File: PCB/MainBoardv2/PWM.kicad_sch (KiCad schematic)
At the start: 14 parts, among them J11 Conn_01x03_Socket, J12 Conn_01x03_Socket, J13 Conn_01x04_Socket, J14 Conn_01x03_Socket, J15 Conn_01x03_Socket, J16 Conn_01x04_Socket, J17 Conn_01x03_Socket, J18 Conn_01x03_Socket, J19 Conn_01x04_Socket, J20 Conn_01x03_Socket, SW3 Slide

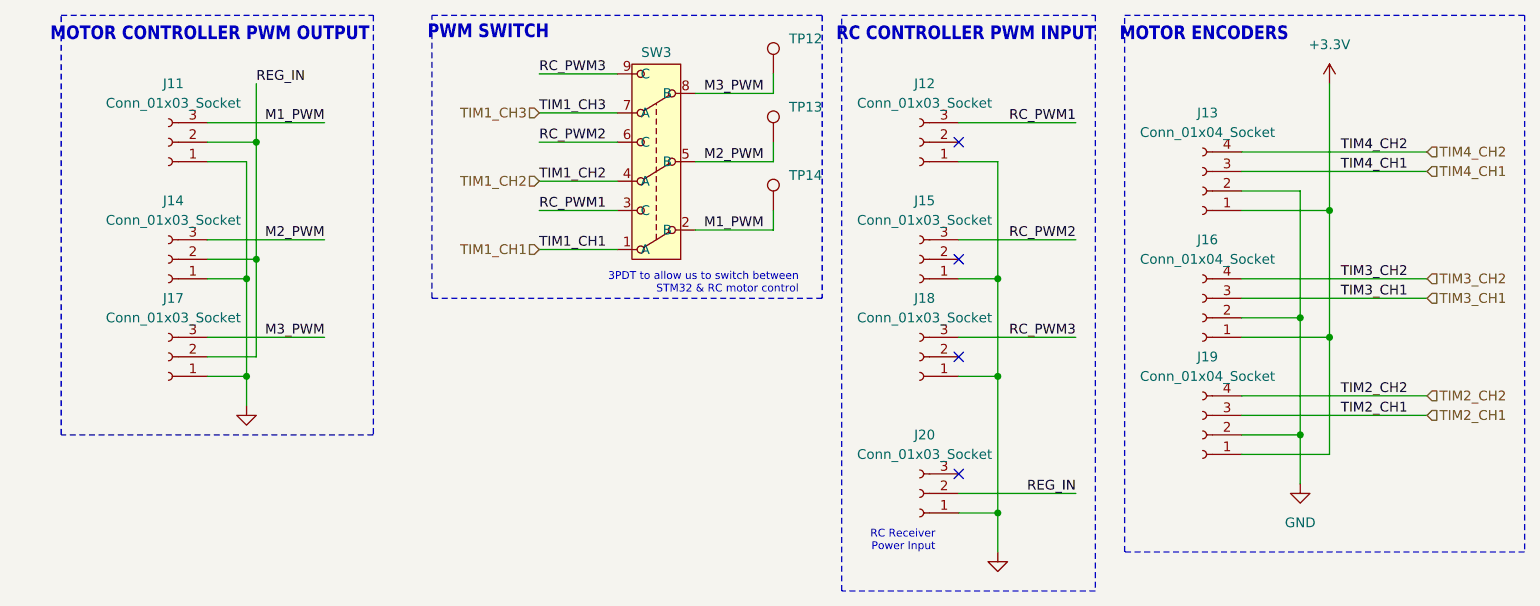
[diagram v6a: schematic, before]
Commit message: Main Board v2 Rough component layout complete
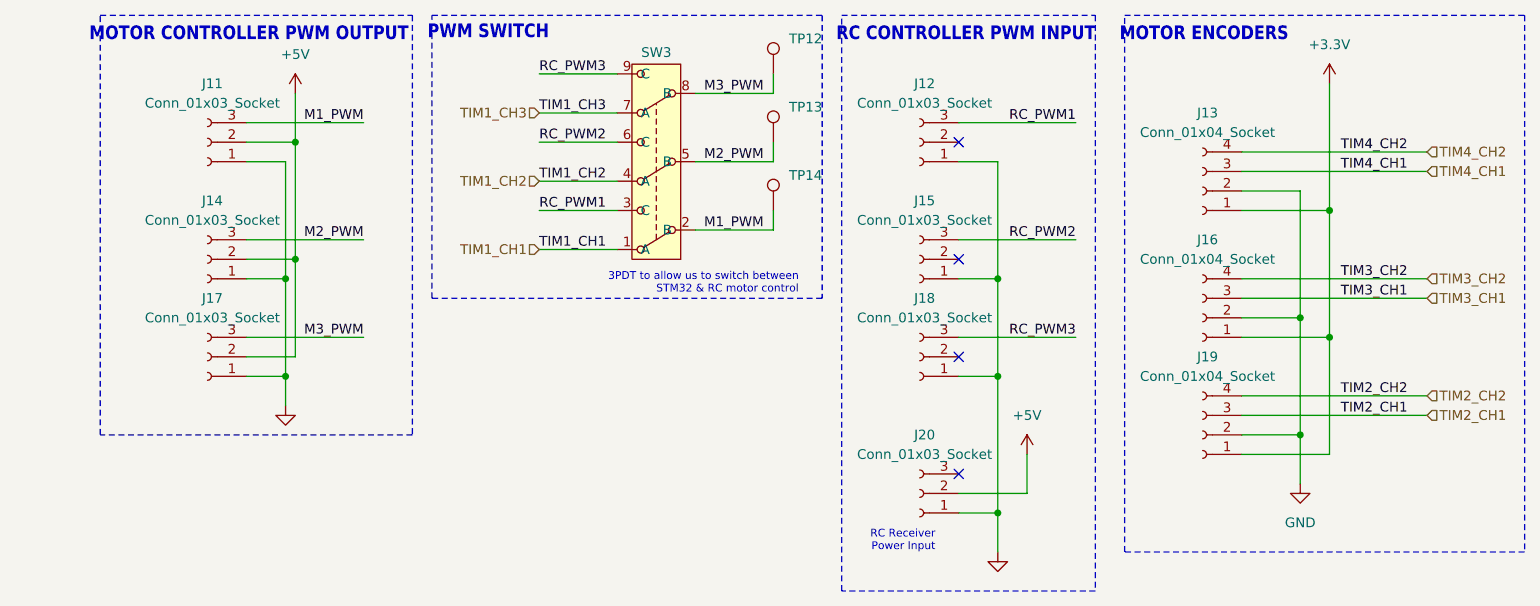
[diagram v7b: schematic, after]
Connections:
- net REG_IN renamed +5V
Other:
- moved on the sheet: J11, J14, J17

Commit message: updating layout progress, adding limit switch extra circuitry
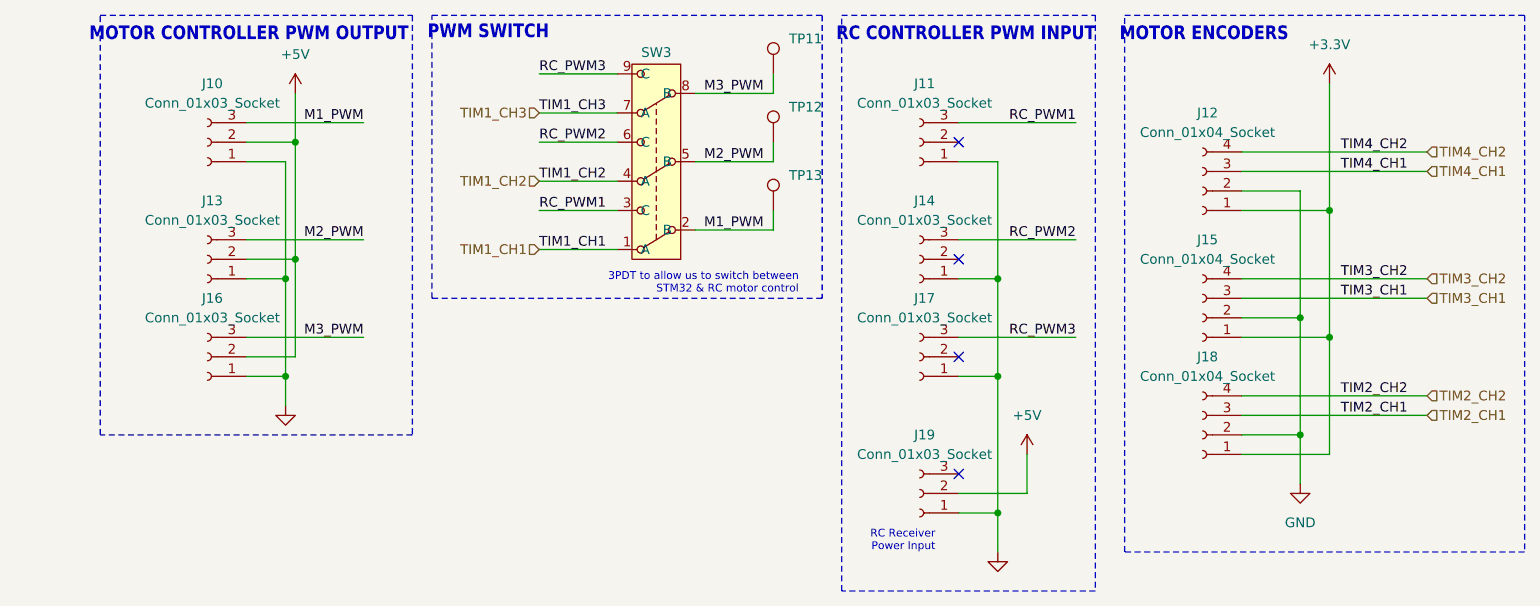
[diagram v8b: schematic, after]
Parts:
- J10: renamed from J11; footprint Connector_PinHeader_2.54mm:PinHeader_1x03_P2.54mm_Vertical -> Connector_PinHeader_2.54mm:PinHeader_1x03_P2.54mm_Horizontal
- J13: renamed from J14; footprint Connector_PinHeader_2.54mm:PinHeader_1x03_P2.54mm_Vertical -> Connector_PinHeader_2.54mm:PinHeader_1x03_P2.54mm_Horizontal
- J16: renamed from J17; footprint Connector_PinHeader_2.54mm:PinHeader_1x03_P2.54mm_Vertical -> Connector_PinHeader_2.54mm:PinHeader_1x03_P2.54mm_Horizontal
- renumbered J12 to J11, J13 to J12, J15 to J14, J16 to J15, J18 to J17, J19 to J18, J20 to J19, TP12 to TP11, TP13 to TP12, TP14 to TP13
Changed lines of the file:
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@@
 		(dnp no)
 		(fields_autoplaced yes)
-		(property "Reference" "J19"
+		(property "Reference" "J18"
 			(at 194.945 104.14 0)
 			(effects
@@
 			(project "MainBoardv2"
 				(path "/d9c43b87-8960-41bd-bfcc-9c305bab2f72/cc711eab-7295-453b-97e2-e692aa39ee0f"
-					(reference "J19")
+					(reference "J18")
 					(unit 1)
 				)
@@
 		(dnp no)
 		(fields_autoplaced yes)
-		(property "Reference" "#PWR040"
+		(property "Reference" "#PWR036"
 			(at 76.2 73.66 0)
 			(effects
@@
 			(project "MainBoardv2"
 				(path "/d9c43b87-8960-41bd-bfcc-9c305bab2f72/cc711eab-7295-453b-97e2-e692aa39ee0f"
-					(reference "#PWR040")
+					(reference "#PWR036")
 					(unit 1)
 				)
@@
 		(dnp no)
 		(fields_autoplaced yes)
-		(property "Reference" "#PWR044"
+		(property "Reference" "#PWR040"
 			(at 167.64 135.89 0)
 			(effects
@@
 			(project "MainBoardv2"
 				(path "/d9c43b87-8960-41bd-bfcc-9c305bab2f72/cc711eab-7295-453b-97e2-e692aa39ee0f"
-					(reference "#PWR044")
+					(reference "#PWR040")
 					(unit 1)
 				)
@@
 		(on_board yes)
 		(dnp no)
-		(property "Reference" "J18"
+		(property "Reference" "J17"
 			(at 158.115 96.52 0)
 			(effects
@@
 			(project "MainBoardv2"
 				(path "/d9c43b87-8960-41bd-bfcc-9c305bab2f72/cc711eab-7295-453b-97e2-e692aa39ee0f"
-					(reference "J18")
+					(reference "J17")
 					(unit 1)
 				)
@@
 		(on_board yes)
 		(dnp no)
-		(property "Reference" "J17"
+		(property "Reference" "J16"
 			(at 65.405 96.52 0)
 			(effects
@@
 			)
 		)
-		(property "Footprint" "Connector_PinHeader_2.54mm:PinHeader_1x03_P2.54mm_Vertical"
+		(property "Footprint" "Connector_PinHeader_2.54mm:PinHeader_1x03_P2.54mm_Horizontal"
 			(at 64.77 104.14 0)
 			(effects
@@
 			(project "MainBoardv2"
 				(path "/d9c43b87-8960-41bd-bfcc-9c305bab2f72/cc711eab-7295-453b-97e2-e692aa39ee0f"
-					(reference "J17")
+					(reference "J16")
 					(unit 1)
 				)
@@
 		(dnp no)
 		(fields_autoplaced yes)
-		(property "Reference" "#PWR042"
+		(property "Reference" "#PWR038"
 			(at 171.45 120.65 0)
 			(effects
@@
 			(project "MainBoardv2"
 				(path "/d9c43b87-8960-41bd-bfcc-9c305bab2f72/cc711eab-7295-453b-97e2-e692aa39ee0f"
-					(reference "#PWR042")
+					(reference "#PWR038")
 					(unit 1)
 				)
@@
 		(dnp no)
 		(fields_autoplaced yes)
-		(property "Reference" "#PWR043"
+		(property "Reference" "#PWR039"
 			(at 207.01 127 0)
 			(effects
@@
 			(project "MainBoardv2"
 				(path "/d9c43b87-8960-41bd-bfcc-9c305bab2f72/cc711eab-7295-453b-97e2-e692aa39ee0f"
-					(reference "#PWR043")
+					(reference "#PWR039")
 					(unit 1)
 				)
@@
 		(on_board yes)
 		(dnp no)
-		(property "Reference" "J12"
+		(property "Reference" "J11"
 			(at 158.115 68.58 0)
 			(effects
@@
 			(project "MainBoardv2"
 				(path "/d9c43b87-8960-41bd-bfcc-9c305bab2f72/cc711eab-7295-453b-97e2-e692aa39ee0f"
-					(reference "J12")
+					(reference "J11")
 					(unit 1)
 				)
@@
 		(dnp no)
 		(fields_autoplaced yes)
-		(property "Reference" "#PWR041"
+		(property "Reference" "#PWR037"
 			(at 74.93 116.84 0)
 			(effects
@@
 			(project "MainBoardv2"
 				(path "/d9c43b87-8960-41bd-bfcc-9c305bab2f72/cc711eab-7295-453b-97e2-e692aa39ee0f"
-					(reference "#PWR041")
+					(reference "#PWR037")
 					(unit 1)
 				)
@@
 		(on_board yes)
 		(dnp no)
-		(property "Reference" "TP13"
+		(property "Reference" "TP12"
 			(at 140.462 71.628 0)
 			(effects
@@
 			(project "MainBoardv2"
 				(path "/d9c43b87-8960-41bd-bfcc-9c305bab2f72/cc711eab-7295-453b-97e2-e692aa39ee0f"
-					(reference "TP13")
+					(reference "TP12")
 					(unit 1)
 				)
@@
 		(dnp no)
 		(fields_autoplaced yes)
-		(property "Reference" "J13"
+		(property "Reference" "J12"
 			(at 194.945 72.39 0)
 			(effects
@@
 			(project "MainBoardv2"
 				(path "/d9c43b87-8960-41bd-bfcc-9c305bab2f72/cc711eab-7295-453b-97e2-e692aa39ee0f"
-					(reference "J13")
+					(reference "J12")
 					(unit 1)
 				)
@@
 		(on_board yes)
 		(dnp no)
-		(property "Reference" "TP12"
+		(property "Reference" "TP11"
 			(at 140.462 62.738 0)
 			(effects
@@
 			(project "MainBoardv2"
 				(path "/d9c43b87-8960-41bd-bfcc-9c305bab2f72/cc711eab-7295-453b-97e2-e692aa39ee0f"
-					(reference "TP12")
+					(reference "TP11")
 					(unit 1)
 				)
@@
 		(on_board yes)
 		(dnp no)
-		(property "Reference" "J20"
+		(property "Reference" "J19"
 			(at 158.115 114.3 0)
 			(effects
@@
 			(project "MainBoardv2"
 				(path "/d9c43b87-8960-41bd-bfcc-9c305bab2f72/cc711eab-7295-453b-97e2-e692aa39ee0f"
-					(reference "J20")
+					(reference "J19")
 					(unit 1)
 				)
@@
 		(on_board yes)
 		(dnp no)
-		(property "Reference" "J15"
+		(property "Reference" "J14"
 			(at 158.115 83.82 0)
 			(effects
@@
 			(project "MainBoardv2"
 				(path "/d9c43b87-8960-41bd-bfcc-9c305bab2f72/cc711eab-7295-453b-97e2-e692aa39ee0f"
-					(reference "J15")
+					(reference "J14")
 					(unit 1)
 				)
@@
 		(dnp no)
 		(fields_autoplaced yes)
-		(property "Reference" "J16"
+		(property "Reference" "J15"
 			(at 194.945 88.9 0)
 			(effects
@@
 			(project "MainBoardv2"
 				(path "/d9c43b87-8960-41bd-bfcc-9c305bab2f72/cc711eab-7295-453b-97e2-e692aa39ee0f"
-					(reference "J16")
+					(reference "J15")
 					(unit 1)
 				)
@@
 		(on_board yes)
 		(dnp no)
-		(property "Reference" "TP14"
+		(property "Reference" "TP13"
 			(at 140.462 80.518 0)
 			(effects
@@
 			(project "MainBoardv2"
 				(path "/d9c43b87-8960-41bd-bfcc-9c305bab2f72/cc711eab-7295-453b-97e2-e692aa39ee0f"
-					(reference "TP14")
+					(reference "TP13")
 					(unit 1)
 				)
@@
 		(on_board yes)
 		(dnp no)
-		(property "Reference" "J14"
+		(property "Reference" "J13"
 			(at 65.405 83.82 0)
 			(effects
@@
 			)
 		)
-		(property "Footprint" "Connector_PinHeader_2.54mm:PinHeader_1x03_P2.54mm_Vertical"
+		(property "Footprint" "Connector_PinHeader_2.54mm:PinHeader_1x03_P2.54mm_Horizontal"
 			(at 64.77 91.44 0)
 			(effects
@@
 			(project "MainBoardv2"
 				(path "/d9c43b87-8960-41bd-bfcc-9c305bab2f72/cc711eab-7295-453b-97e2-e692aa39ee0f"
-					(reference "J14")
+					(reference "J13")
 					(unit 1)
 				)
@@
 		(on_board yes)
 		(dnp no)
-		(property "Reference" "J11"
+		(property "Reference" "J10"
 			(at 65.405 68.58 0)
 			(effects
@@
 			)
 		)
-		(property "Footprint" "Connector_PinHeader_2.54mm:PinHeader_1x03_P2.54mm_Vertical"
+		(property "Footprint" "Connector_PinHeader_2.54mm:PinHeader_1x03_P2.54mm_Horizontal"
 			(at 64.77 76.2 0)
 			(effects
@@
 			(project "MainBoardv2"
 				(path "/d9c43b87-8960-41bd-bfcc-9c305bab2f72/cc711eab-7295-453b-97e2-e692aa39ee0f"
-					(reference "J11")
+					(reference "J10")
 					(unit 1)
 				)
@@
 		(dnp no)
 		(fields_autoplaced yes)
-		(property "Reference" "#PWR039"
+		(property "Reference" "#PWR035"
 			(at 210.82 72.39 0)
 			(effects
@@
 			(project "MainBoardv2"
 				(path "/d9c43b87-8960-41bd-bfcc-9c305bab2f72/cc711eab-7295-453b-97e2-e692aa39ee0f"
-					(reference "#PWR039")
-					(unit 1)
-				)
+					(reference "#PWR035")
+					(unit 1)
+				)
